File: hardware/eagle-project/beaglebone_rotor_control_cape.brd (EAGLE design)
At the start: 83.8 x 62.6 mm, 52 parts, among them IC1 TLC2264CDU, IC2 MCP4901, IC6 TLC2264CDU, Q1 SQ2348ES-T1-GE3, Q2 SQ2348ES-T1-GE3, Q3 SQ2348ES-T1-GE3, Q4 SQ2348ES-T1-GE3, Q5 SQ2348ES-T1-GE3, Q6 SQ2348ES-T1-GE3, U1 TMH0512S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

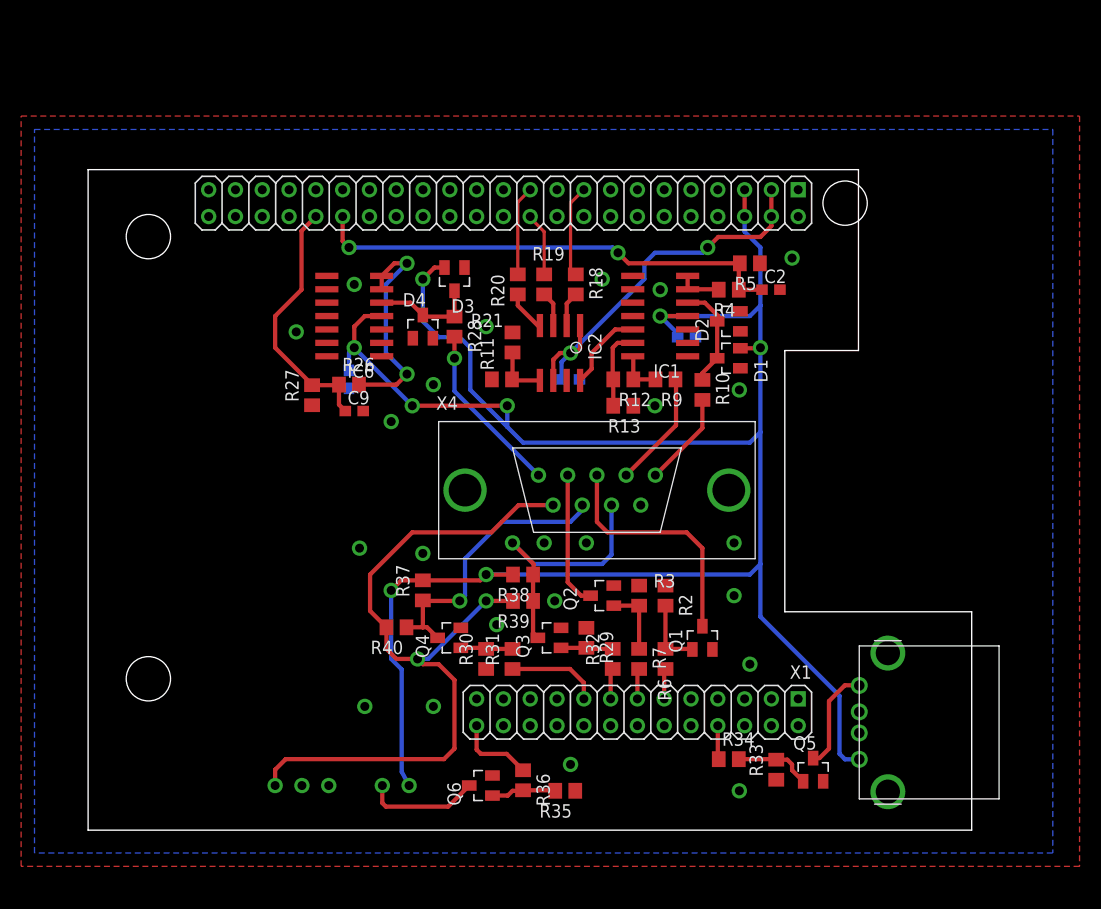
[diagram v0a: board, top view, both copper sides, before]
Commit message: Tweaked eagle layout for easier manufacturing
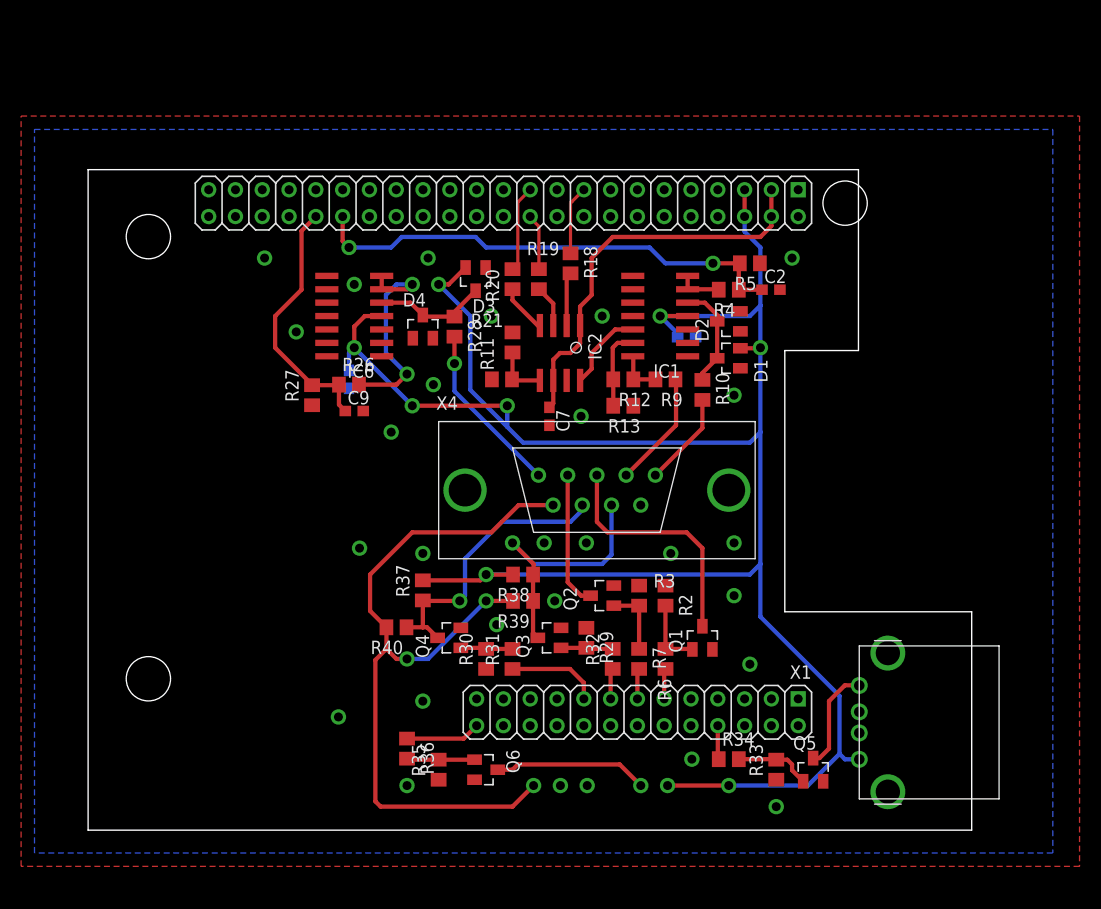
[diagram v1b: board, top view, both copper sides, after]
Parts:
- moved U1 24.5 mm to (43.5, -2.50)
- moved R35 12.2 mm to (34.5, -1.00), turned to 90 degrees
- moved R36 11.4 mm to (31.5, 1.00)
- moved C7 4.03 mm to (45.0, 32.5), flipped to the top, turned to 270 degrees
- moved R18 2.06 mm to (47.0, 47.0)
- moved D3 2.00 mm to (38.0, 45.5)
- moved Q6 1.58 mm to (39.0, -1.00), turned to 270 degrees
- moved R19 0.71 mm to (44.0, 45.5)
- moved R20 0.71 mm to (41.5, 45.5)
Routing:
- net +5V: track 206.3 -> 199.7 mm
- net N$37: track 10.9 -> 14.6 mm
- net BB_SPI0_CS0: track 9.05 -> 6.55 mm
- net N$6: track 3.31 -> 5.47 mm
- net BB_AIN_H: track 45.7 -> 46.5 mm
- net N$36: track 9.90 -> 10.7 mm
- net +12V: track 72.6 -> 73.4 mm
- net N$35: track 21.3 -> 20.6 mm
- net N$9: track 3.93 -> 4.64 mm
- net N$10: track 3.31 -> 4.02 mm
- net BB_SPI0_SCLK: track 6.03 -> 5.32 mm
- net +3V3: track 38.3 -> 38.1 mm, vias 2 -> 0

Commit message: Added serial interface chip to layout
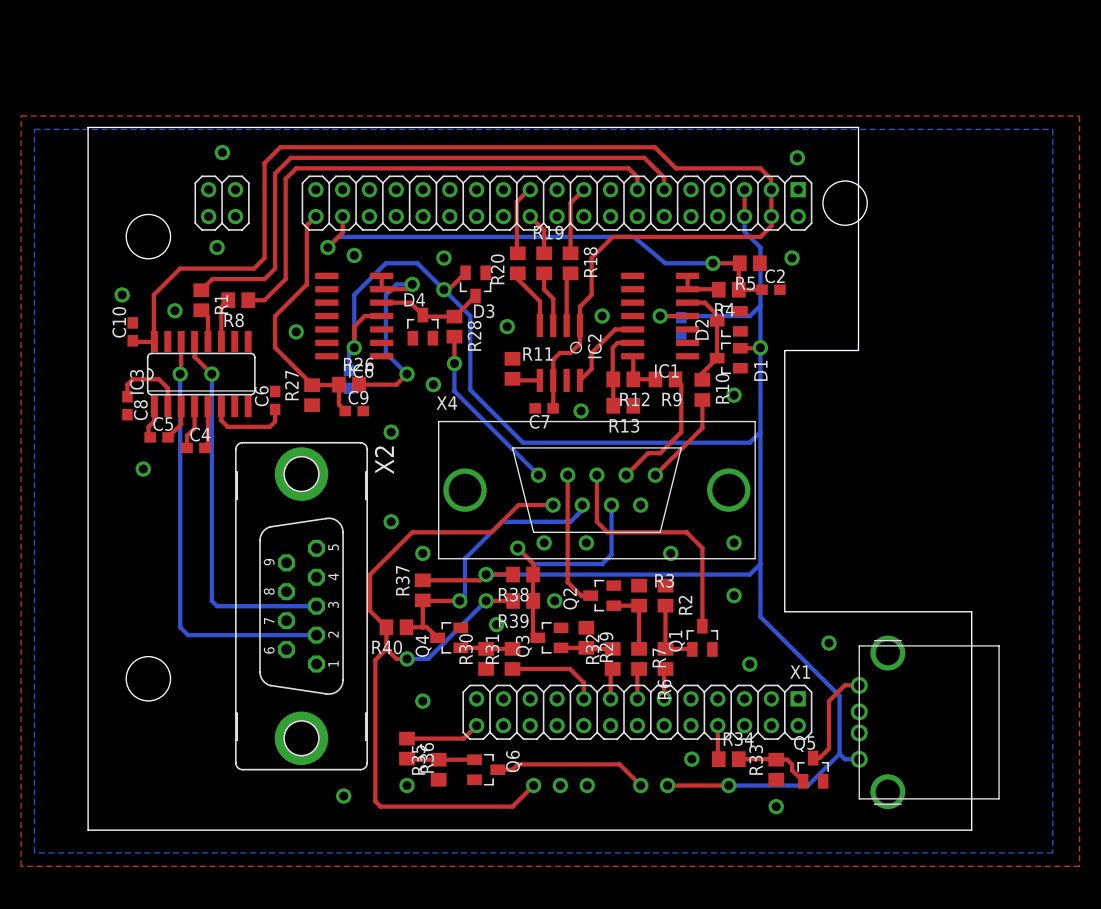
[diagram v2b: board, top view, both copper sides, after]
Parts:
- removed R21: 100, rcl:R0805
- added C10, C4, C5, C6, C8: 100n, rcl:C0603
- added IC3: MAX3232ESE, maxim:SO16
- added R1, R8: 100, rcl:R0805
- added X2: (no value), con-subd:F09VP
- moved R19 1.58 mm to (44.5, 47.0)
- moved R20 1.58 mm to (42.0, 47.0)
- moved R11 1.41 mm to (41.5, 37.0), turned to 270 degrees
- moved C3 1.12 mm to (57.5, 41.0), turned to 270 degrees
- moved C7 0.90 mm to (44.5, 33.2), turned to 180 degrees
- moved D3 0.50 mm to (38.0, 45.0)
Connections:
- removed net AIN0: X1.85
- removed net BB_SPI0_D1: X1.64
- removed net BB_SPI1_CS0: X1.74
- removed net BB_SPI1_D0: X1.75
- removed net BB_SPI1_D1: X1.76
- removed net BB_SPI1_SCLK: X1.77
- removed net N$41: X1.19
- removed net N$42: X1.16
- removed net N$4243: X1.18
- removed net N$43: X1.14
- removed net N$44: X1.12
- removed net N$8: R21.1
- new net BB_UART4_RX: R1.1, X1.57
- new net BB_UART4_TX: R8.1, X1.59
- new net N$16: C4.1, IC3.4
- new net N$17: C4.2, IC3.5
- new net N$18: C5.2, IC3.3
- new net N$19: C5.1, IC3.1
- new net N$20: C6.1, IC3.6
- new net N$21: C8.1, IC3.2
- new net N$22: IC3.11, R8.2
- new net N$25: IC3.12, R1.2
- new net RS232_RX: IC3.13, X2.3
- new net RS232_TX: IC3.14, X2.2
- net +3V3: now also C10.1, IC3.16
- net GND: now also C10.2, C6.2, C8.2, IC3.15, X2.5
- net N$7: no longer R21.2
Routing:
- net +3V3: track 38.1 -> 116.5 mm
- net BB_UART4_RX: track 0.00 -> 56.3 mm
- net BB_UART4_TX: track 0.00 -> 49.2 mm
- net RS232_TX: track 0.00 -> 40.3 mm, vias 0 -> 1
- net RS232_RX: track 0.00 -> 35.4 mm, vias 0 -> 1
- net N$20: track 0.00 -> 8.03 mm
- net N$21: track 0.00 -> 7.27 mm
- net +5V: track 199.7 -> 193.5 mm, vias 8 -> 6
- net N$16: track 0.00 -> 4.22 mm
- net N$22: track 0.00 -> 4.19 mm
- net N$17: track 0.00 -> 4.04 mm
- net N$18: track 0.00 -> 3.44 mm
- net N$25: track 0.00 -> 3.24 mm
- net N$19: track 0.00 -> 3.22 mm
- net N$7: track 5.26 -> 2.70 mm
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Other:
- board size 83.8 x 62.6 mm -> 83.8 x 66.6 mm

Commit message: Eagle layout update finalized for manufacturing
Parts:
- moved C7 2.00 mm to (44.5, 35.2)
- moved IC2 2.00 mm to (46.0, 40.5)
- moved R11 2.00 mm to (41.5, 39.0)
- moved X2 1.00 mm to (20.5, 14.5)
- moved R18 0.50 mm to (47.0, 47.5)
- moved R19 0.50 mm to (44.5, 47.5)
- moved R20 0.50 mm to (42.0, 47.5)
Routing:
- net +3V3: track 116.5 -> 114.5 mm
- net N$6: track 5.47 -> 3.60 mm
- net N$2: track 7.88 -> 6.17 mm
- net N$10: track 5.31 -> 3.81 mm
- net N$9: track 5.82 -> 4.32 mm
- net RS232_TX: track 40.3 -> 39.3 mm
- net RS232_RX: track 35.4 -> 34.4 mm
- net BB_SPI0_SCLK: track 4.03 -> 3.53 mm
- net BB_SPI0_CS0: track 6.55 -> 6.05 mm
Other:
- outline, holes or cut-outs redrawn
